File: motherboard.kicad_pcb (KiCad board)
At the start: 2 copper layers, 91 parts, among them P1 CONN_01X08, P2 CONN_01X08, P3 CONN_02X26, P4 CONN_02X26, U1 STM32F411-LQFP64, U10 74LS125, U11 74LS125, U12 74LS125, U13 74LS125, U14 PCA9517A, U15 PCA9517A, U16 74LS125, U17 74LS125, U2 STM32F411-LQFP64, U3 AP7313, U4 74LS00, U5 74LS125, U6 FM25V20A-G, U7 FM25V20A-G, U8 FM25V20A-G, U9 FM25V20A-G, Y1 32k, Y2 8M(16pF), Y3 32k, Y4 8M(16pF)

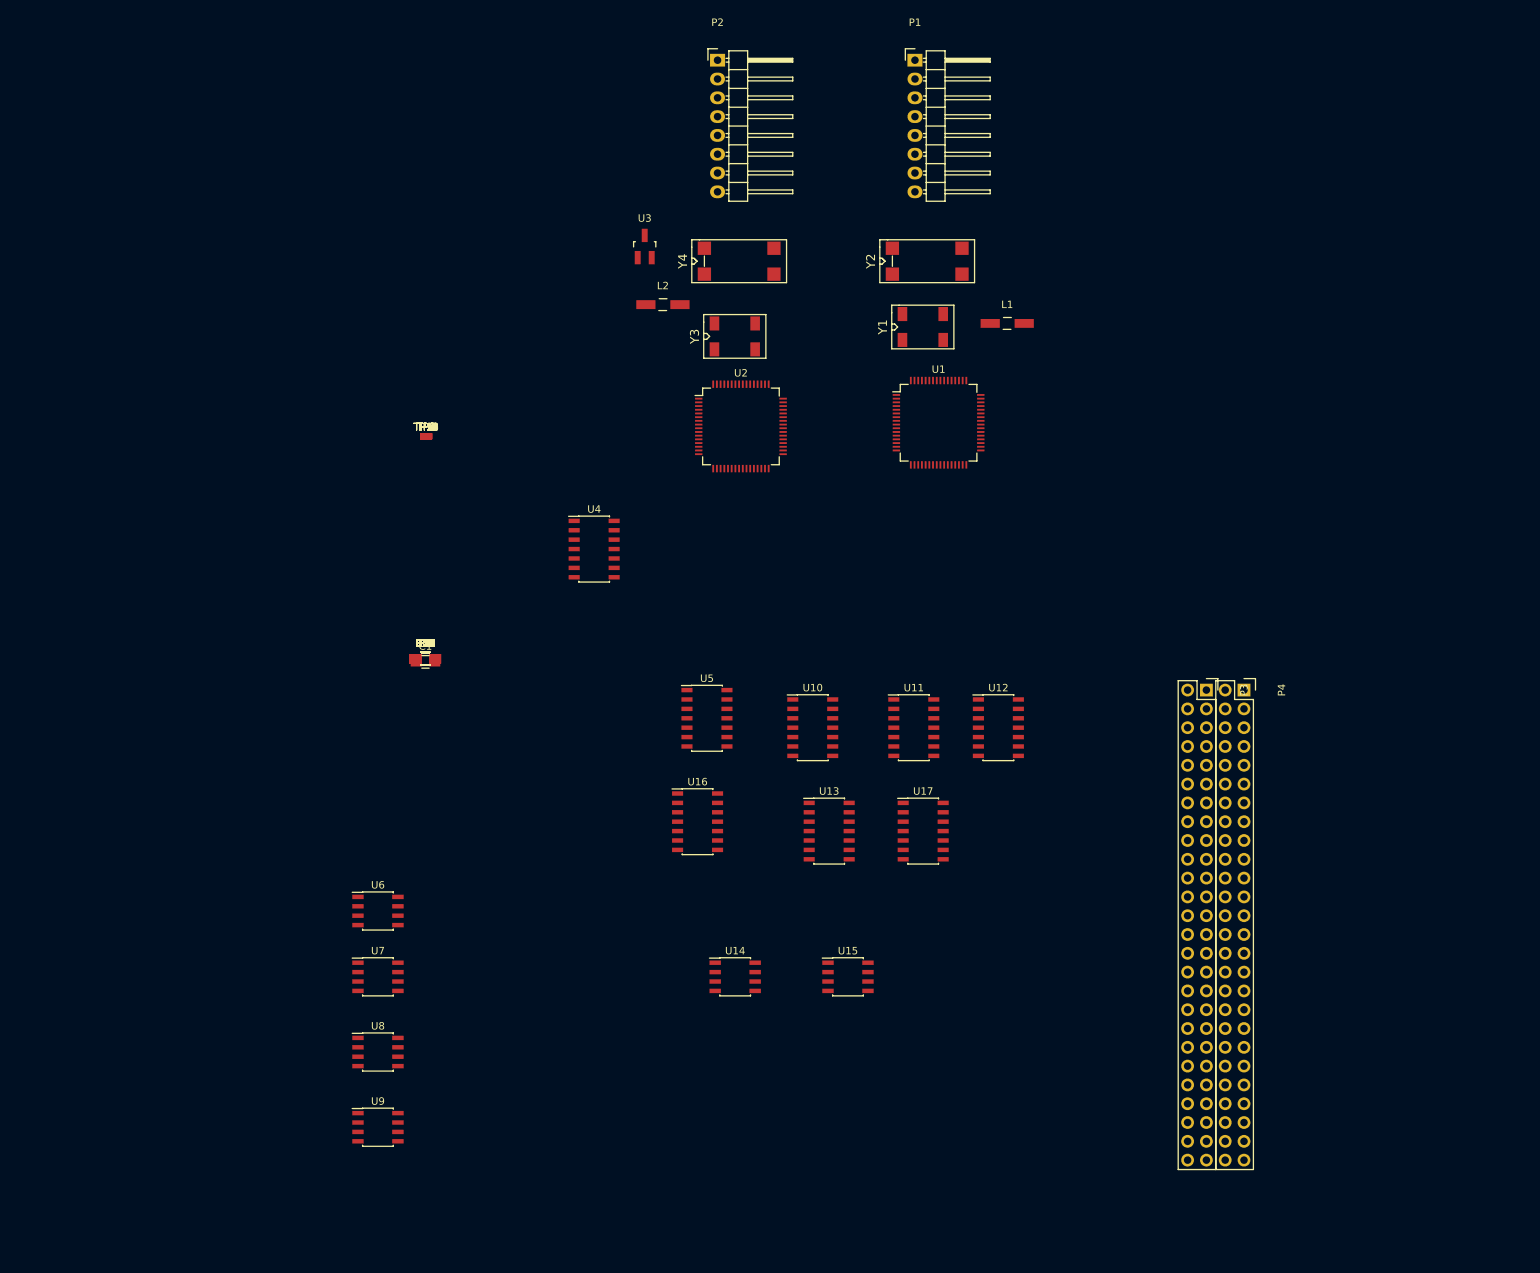
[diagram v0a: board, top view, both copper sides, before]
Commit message: Finished board outline and connector placement
Beginning to assign GPIOs and layout components
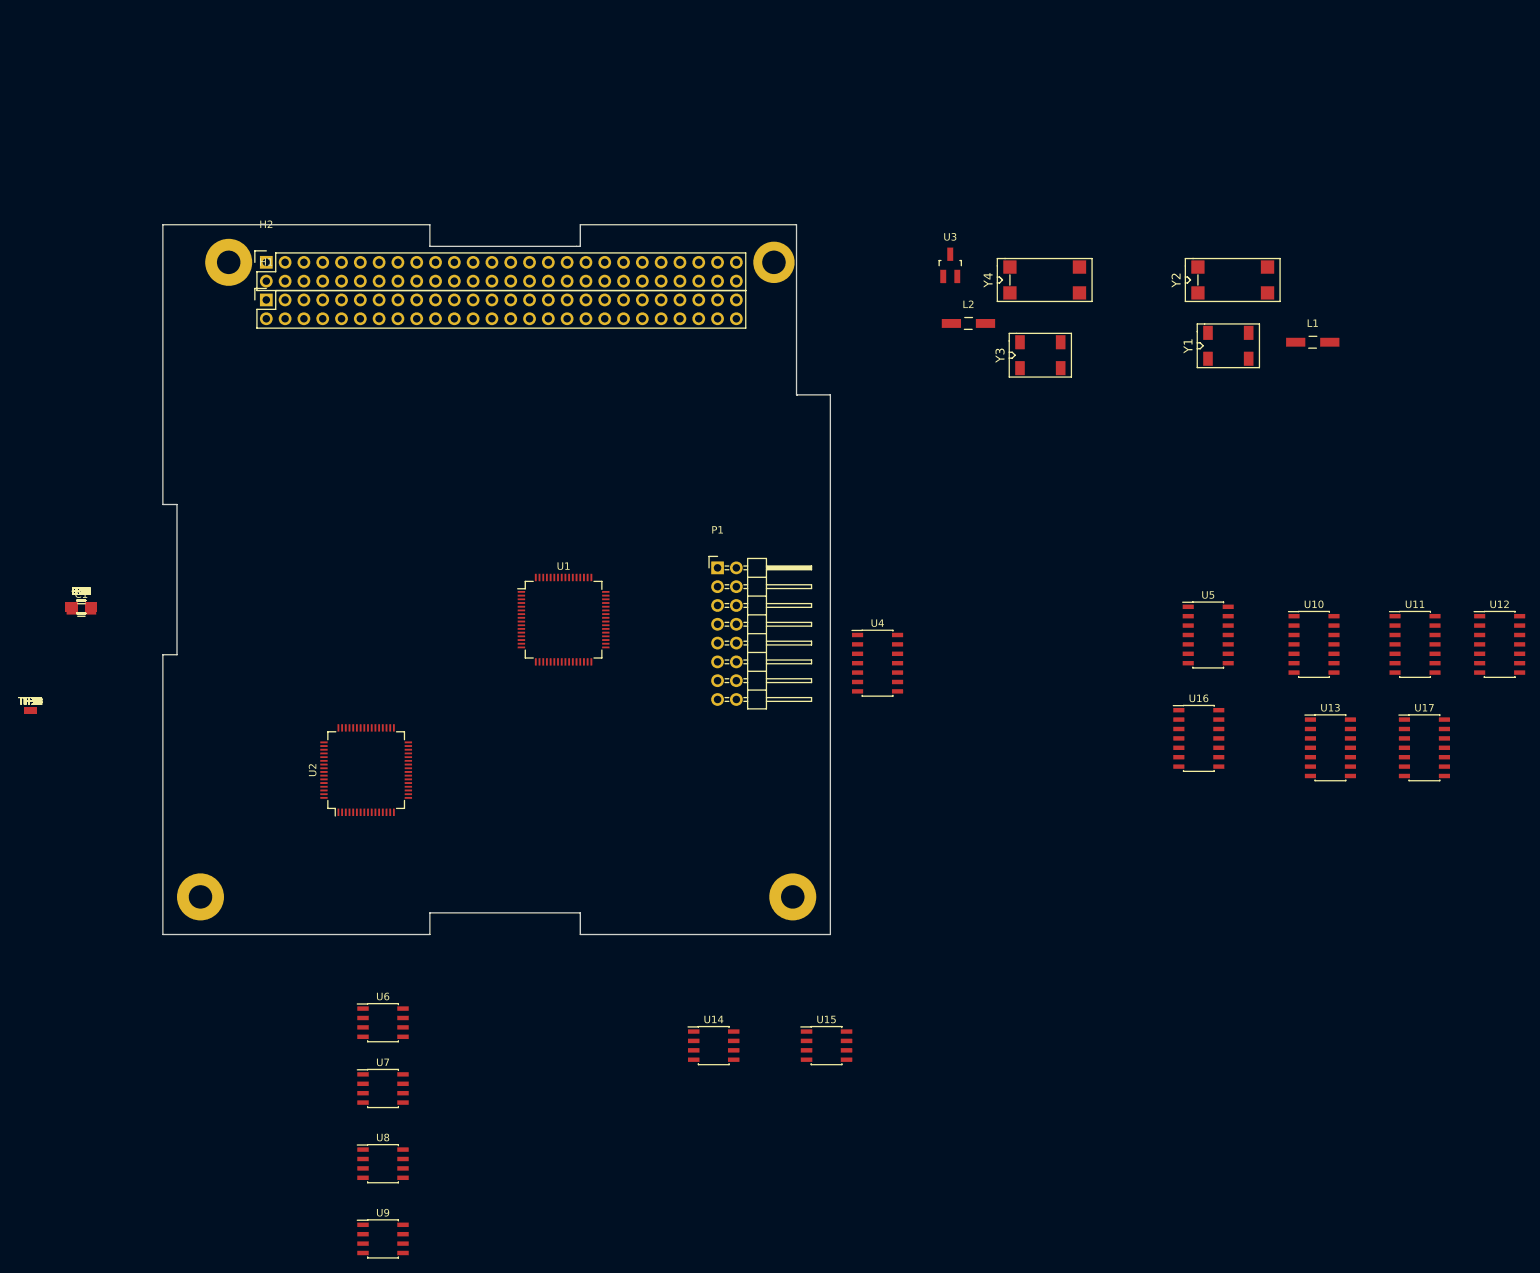
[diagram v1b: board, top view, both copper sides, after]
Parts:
- removed P2: CONN_01X08, Pin_Headers:Pin_Header_Angled_1x08
- removed P3, P4: CONN_02X26, Socket_Strips:Socket_Strip_Straight_2x26
- added H1: CONN_02X26, Socket_Strips:Socket_Strip_Straight_2x26, F.Cu at (127.0, 56.5)
- added H2: CONN_02X26, Socket_Strips:Socket_Strip_Straight_2x26, F.Cu at (127.0, 51.4)
- added REF**: Hole_0.125-0.250, motherboard:Hole_0.125-0.250, F.Cu at (118.1, 137.2)
- added REF**: Hole_0.125-0.250, motherboard:Hole_0.125-0.250, F.Cu at (198.1, 137.2)
- added REF**: Hole_0.125-0.250, motherboard:Hole_0.125-0.250, F.Cu at (195.6, 51.4)
- added REF**: Hole_0.125-0.250, motherboard:Hole_0.125-0.250, F.Cu at (121.9, 51.4)
- P1: value CONN_01X08 -> CONN_02X08; footprint Pin_Headers:Pin_Header_Angled_1x08 -> Pin_Headers:Pin_Header_Angled_2x08
- moved P1 73.6 mm to (188.0, 92.7)
- moved U2 68.7 mm to (140.5, 120.0), turned to 90 degrees
- moved U10 68.6 mm to (268.5, 103.0)
- moved U16 68.6 mm to (253.0, 115.7)
- moved U11 68.6 mm to (282.2, 103.0)
- moved U12 68.6 mm to (293.6, 103.0)
- moved U13 68.6 mm to (270.8, 117.0)
- moved U5 68.6 mm to (254.2, 101.8)
- moved U17 68.6 mm to (283.5, 117.0)
- moved TP1 65.0 mm to (95.2, 112.0)
- moved TP10 65.0 mm to (95.2, 112.0)
- moved TP11 65.0 mm to (95.2, 112.0)
- moved TP12 65.0 mm to (95.2, 112.0)
- moved TP13 65.0 mm to (95.2, 112.0)
- moved TP14 65.0 mm to (95.2, 112.0)
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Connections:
- P1 pad 2: /TMS_P -> GND
- P1 pad 3: /TCK_P -> /TMS_P
- P1 pad 4: /SWO_P -> /TMS_S
- P1 pad 5: /UART2_TX -> /TCK_P
- P1 pad 6: /UART2_RX -> /TCK_S
- P1 pad 7: /NRST_P -> /SWO_P
- P1 pad 8: GND -> /SWO_S
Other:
- board outline added: 90.2 x 95.9 mm

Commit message: Progress in laying out components
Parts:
- moved U17 143.9 mm to (139.5, 119.4)
- moved U13 143.8 mm to (127.0, 119.4)
- moved L1 137.8 mm to (137.2, 104.4), turned to 270 degrees
- moved U11 130.8 mm to (152.4, 119.4)
- moved Y1 125.8 mm to (135.4, 95.0), turned to 270 degrees
- moved Y2 125.8 mm to (135.4, 83.8), turned to 90 degrees
- moved U10 120.8 mm to (152.4, 69.8)
- moved U5 118.9 mm to (139.7, 69.8)
- moved U12 116.8 mm to (178.0, 119.4)
- moved U15 96.9 mm to (165.1, 67.9)
- moved Y4 95.3 mm to (154.1, 108.4), turned to 180 degrees
- moved U14 89.8 mm to (177.8, 67.9)
- moved U16 88.0 mm to (165.1, 119.4)
- moved Y3 79.1 mm to (166.2, 108.4)
- moved U9 71.0 mm to (190.5, 130.8)
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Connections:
- H1 pad 10: Net-(H1-Pad10) -> /GPIO7
- H1 pad 12: Net-(H1-Pad12) -> /GPIO9
- H1 pad 14: Net-(H1-Pad14) -> /GPIO11
- H1 pad 16: Net-(H1-Pad16) -> /GPIO13
- H1 pad 18: Net-(H1-Pad18) -> /RADIO_TX
- H1 pad 2: Net-(H1-Pad2) -> /GPIO1
- H1 pad 20: Net-(H1-Pad20) -> /I2C2_SCL
- H1 pad 22: Net-(H1-Pad22) -> /SYS_SPI_MISO
- H1 pad 24: Net-(H1-Pad24) -> /SYS_SPI_NSS
- H1 pad 29: Net-(H1-Pad29) -> /SYS_RESET
- H1 pad 33: Net-(H1-Pad33) -> /SGPIO7
- H1 pad 34: Net-(H1-Pad34) -> /SGPIO8
- H1 pad 35: Net-(H1-Pad35) -> /SGPIO9
- H1 pad 36: Net-(H1-Pad36) -> /SGPIO10
- H1 pad 37: Net-(H1-Pad37) -> /SGPIO11
- H1 pad 38: Net-(H1-Pad38) -> /SGPIO12
- H1 pad 39: Net-(H1-Pad39) -> /SGPIO13
- H1 pad 4: Net-(H1-Pad4) -> /GPIO3
- H1 pad 40: Net-(H1-Pad40) -> /SGPIO14
- H1 pad 41: Net-(H1-Pad41) -> /SYS_SDA
- H1 pad 43: Net-(H1-Pad43) -> /SYS_SCL
- H1 pad 47: Net-(H1-Pad47) -> /NBUFEN_PRI
- H1 pad 48: Net-(H1-Pad48) -> /NBUFEN_SEC
- H1 pad 49: Net-(H1-Pad49) -> /I2C2_SDA
- H1 pad 50: Net-(H1-Pad50) -> /SGPIO5
- H1 pad 51: Net-(H1-Pad51) -> /I2C2_SCL
- H1 pad 52: Net-(H1-Pad52) -> /SGPIO6
- H1 pad 6: Net-(H1-Pad6) -> /RADIO_RR
- H1 pad 8: Net-(H1-Pad8) -> /GPIO5
- H2 pad 1: Net-(H2-Pad1) -> /SGPIO0
- H2 pad 14: Net-(H2-Pad14) -> GND
- H2 pad 17: Net-(H2-Pad17) -> GND
- H2 pad 2: Net-(H2-Pad2) -> /SGPIO1
- H2 pad 21: Net-(H2-Pad21) -> GND
- H2 pad 22: Net-(H2-Pad22) -> GND
- H2 pad 25: Net-(H2-Pad25) -> +5V
- H2 pad 26: Net-(H2-Pad26) -> +5V
- H2 pad 27: Net-(H2-Pad27) -> +3V3
- H2 pad 28: Net-(H2-Pad28) -> +3V3
- H2 pad 29: Net-(H2-Pad29) -> GND
- H2 pad 3: Net-(H2-Pad3) -> /SGPIO2
- H2 pad 30: Net-(H2-Pad30) -> GND
- H2 pad 32: Net-(H2-Pad32) -> GND
- H2 pad 4: Net-(H2-Pad4) -> /SGPIO3
- H2 pad 47: Net-(H2-Pad47) -> GND
- H2 pad 48: Net-(H2-Pad48) -> GND
- H2 pad 49: Net-(H2-Pad49) -> /SPI2_NSS
- H2 pad 5: Net-(H2-Pad5) -> /I2C3_SDA
- H2 pad 50: Net-(H2-Pad50) -> /SPI2_SCK
- H2 pad 51: Net-(H2-Pad51) -> /SPI2_MISO
- H2 pad 52: Net-(H2-Pad52) -> /SPI2_MOSI
- H2 pad 6: Net-(H2-Pad6) -> /I2C3_SCL
- H2 pad 7: Net-(H2-Pad7) -> /SGPIO4
- H2 pad 9: Net-(H2-Pad9) -> GND
- U1 pad 54: /GPIO15 -> /GPIO13
- U10 pad 11: Net-(U10-Pad11) -> /RADIO_TX
- U10 pad 12: /RADIO_RR -> /RADIO_TX_S
- U10 pad 13: GND -> /NBUFEN_SEC
- U10 pad 5: /MEM_MISO -> /RADIO_TR
- U10 pad 6: /MEM_MISO_S -> /RADIO_TR_S
- U10 pad 8: /RADIO_TR_S -> /RADIO_RR_S
- U10 pad 9: Net-(U10-Pad9) -> /RADIO_RR
- U11 pad 1: /NBUFEN_PRI -> GND
- U11 pad 11: /MEM_CS2 -> /SYS_RESET
- U11 pad 12: /MEM_CS2_P -> /SYS_RESET_P
- U11 pad 2: /MEM_NHOLD_P -> /MEM_MISO
- U11 pad 3: /MEM_NHOLD -> /MEM_MISO_P
- U11 pad 5: /MEM_NWP_P -> /MEM_SCK_P
- U11 pad 6: /MEM_NWP -> /MEM_SCK
- U11 pad 8: /MEM_CS3 -> /MEM_MOSI
- U11 pad 9: /MEM_CS3_P -> /MEM_MOSI_P
- U12 pad 1: /NBUFEN_PRI -> GND
- U12 pad 10: /NBUFEN_PRI -> /NBUFEN_SEC
- U12 pad 11: /MEM_MOSI -> /SYS_RESET
- U12 pad 12: /MEM_MOSI_P -> /SYS_RESET_S
- U12 pad 13: /NBUFEN_PRI -> /NBUFEN_SEC
- U12 pad 2: /MEM_CS1_P -> /MEM_MISO
- U12 pad 3: /MEM_CS1 -> /MEM_MISO_S
- U12 pad 4: /NBUFEN_PRI -> /NBUFEN_SEC
- U12 pad 5: /MEM_CS0_P -> /MEM_SCK_S
- U12 pad 6: /MEM_CS0 -> /MEM_SCK
- U12 pad 8: /MEM_SCK -> /MEM_MOSI
- U12 pad 9: /MEM_SCK_P -> /MEM_MOSI_S
- U13 pad 2: /RADIO_TX_P -> /MEM_NHOLD_P
- U13 pad 3: /RADIO_TX -> /MEM_NHOLD
- U13 pad 5: /SYS_RESET_P -> /MEM_NWP_P
- U13 pad 6: /SYS_RESET -> /MEM_NWP
- U17 pad 1: /NBUFEN_SEC -> /NBUFEN_PRI
- U17 pad 10: /NBUFEN_SEC -> /NBUFEN_PRI
- U17 pad 11: /SYS_RESET -> /MEM_CS0
- U17 pad 12: /SYS_RESET_S -> /MEM_CS0_P
- U17 pad 13: /NBUFEN_SEC -> /NBUFEN_PRI
- U17 pad 2: /MEM_SCK_S -> /MEM_CS3_P
- U17 pad 3: /MEM_SCK -> /MEM_CS3
- U17 pad 4: /NBUFEN_SEC -> /NBUFEN_PRI
- U17 pad 5: /MEM_MOSI_S -> /MEM_CS2_P
- U17 pad 6: /MEM_MOSI -> /MEM_CS2
- U17 pad 8: /RADIO_TX -> /MEM_CS1
- U17 pad 9: /RADIO_TX_S -> /MEM_CS1_P
- U2 pad 10: /SGPIO_4 -> /SGPIO4
- U2 pad 11: /SGPIO_5 -> /SGPIO5
- U2 pad 54: /SGPIO16 -> /SGPIO14
- U5 pad 11: Net-(U5-Pad11) -> /RADIO_TX
- U5 pad 12: /RADIO_RR -> /RADIO_TX_P
- U5 pad 13: GND -> /NBUFEN_PRI
- U5 pad 5: /MEM_MISO -> /RADIO_TR
- U5 pad 6: /MEM_MISO_P -> /RADIO_TR_P
- U5 pad 8: /RADIO_TR_P -> /RADIO_RR_P
- U5 pad 9: Net-(U5-Pad9) -> /RADIO_RR
- U6 pad 4: Net-(U6-Pad4) -> GND
- U7 pad 4: Net-(U7-Pad4) -> GND
- U8 pad 4: Net-(U8-Pad4) -> GND
- U9 pad 4: Net-(U9-Pad4) -> GND

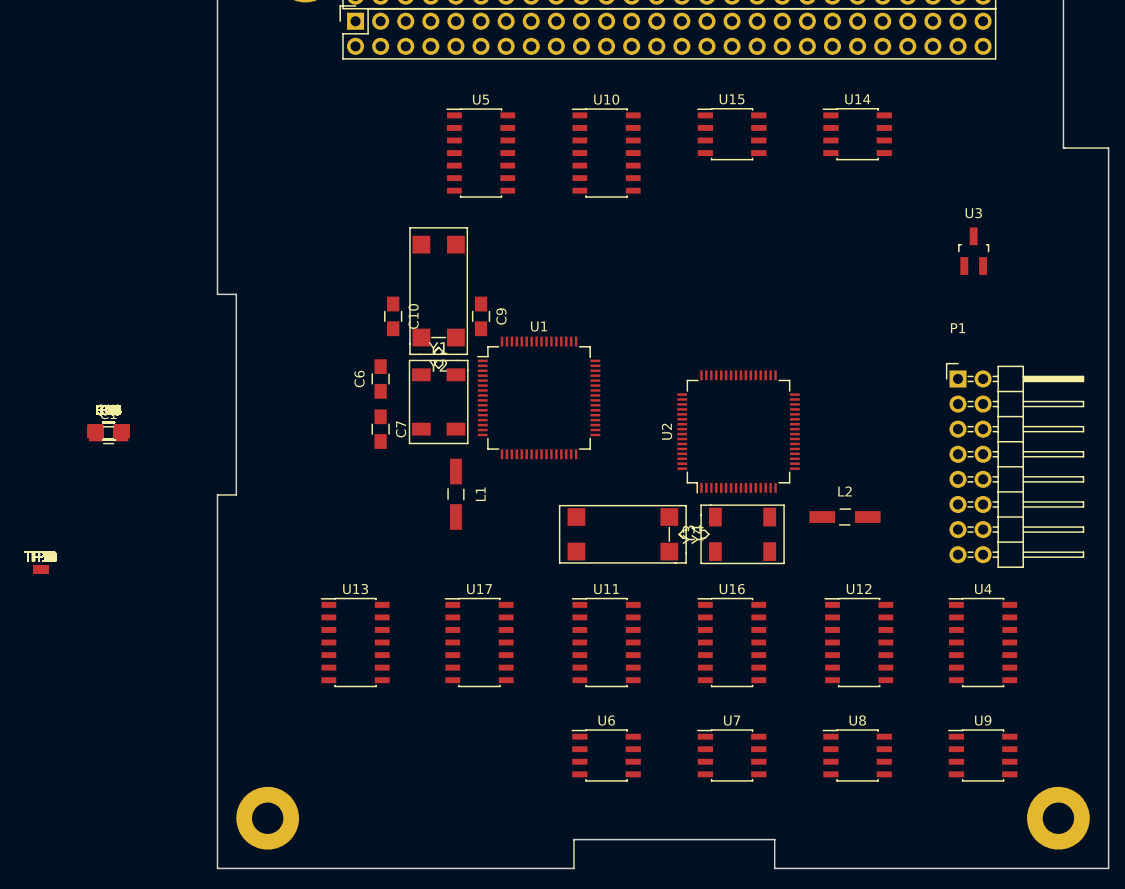
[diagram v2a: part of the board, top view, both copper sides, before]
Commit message: Placed all components
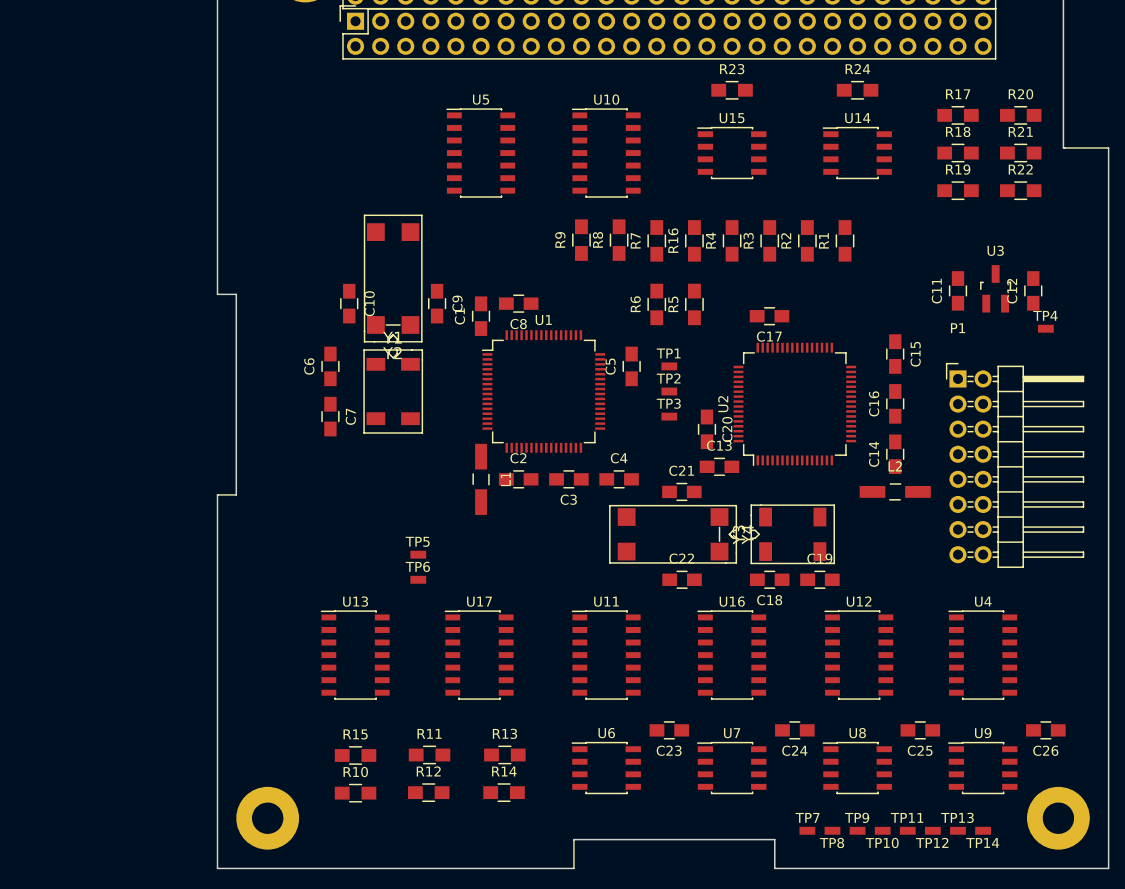
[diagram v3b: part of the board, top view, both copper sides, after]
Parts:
- moved TP4 104.6 mm to (196.8, 87.6)
- moved C26 99.5 mm to (196.8, 128.3), turned to 180 degrees
- moved TP14 98.9 mm to (190.5, 138.4)
- moved R20 97.7 mm to (194.3, 66.0)
- moved R21 96.5 mm to (194.3, 69.8)
- moved TP13 96.5 mm to (188.0, 138.4)
- moved R22 95.4 mm to (194.3, 73.7)
- moved C12 94.6 mm to (195.6, 83.8), turned to 90 degrees
- moved TP12 94.0 mm to (185.4, 138.4)
- moved R17 91.7 mm to (188.0, 66.0)
- moved TP11 91.6 mm to (182.9, 138.4)
- moved R18 90.4 mm to (188.0, 69.8)
- moved R19 89.3 mm to (188.0, 73.7)
- moved TP10 89.2 mm to (180.3, 138.4)
- moved C25 87.5 mm to (184.2, 128.3), turned to 180 degrees
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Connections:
- R15 pad 1: Net-(R15-Pad1) -> +3V3
- R15 pad 2: +3V3 -> Net-(R15-Pad2)
- R17 pad 1: +3V3 -> /NBUFEN_SEC
- R17 pad 2: /NBUFEN_SEC -> +3V3
- R19 pad 1: +3V3 -> /SYS_SCL_P
- R19 pad 2: /SYS_SCL_P -> +3V3
- R20 pad 1: +3V3 -> /SYS_SDA_P
- R20 pad 2: /SYS_SDA_P -> +3V3
- R21 pad 1: +3V3 -> /SYS_SCL_S
- R21 pad 2: /SYS_SCL_S -> +3V3
- R22 pad 1: +3V3 -> /SYS_SDA_S
- R22 pad 2: /SYS_SDA_S -> +3V3
- R7 pad 1: GND -> /BOOT0_S
- R7 pad 2: /BOOT0_S -> GND
- R8 pad 1: GND -> /BOOT0_P
- R8 pad 2: /BOOT0_P -> GND
- U1 pad 43: GND -> /PRX_STX
- U1 pad 63: (no net) -> GND
- U2 pad 43: GND -> /PTX_SRX
- U2 pad 63: (no net) -> GND
- U6 pad 7: Net-(R15-Pad1) -> Net-(R15-Pad2)
- U7 pad 7: Net-(R15-Pad1) -> Net-(R15-Pad2)
- U8 pad 7: Net-(R15-Pad1) -> Net-(R15-Pad2)
- U9 pad 7: Net-(R15-Pad1) -> Net-(R15-Pad2)
